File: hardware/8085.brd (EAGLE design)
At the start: 167.9 x 122.5 mm, 52 parts, among them IC10 74HCT00N, IC11 74HCT245DW, IC2 74AC573N, IC3 ATF16V8BP3, IC4 74AC00D, IC5 74HCT245DW, IC6 74AC273N, IC7 74HCT139N, IC8 7404N, IC9 74HCT138N

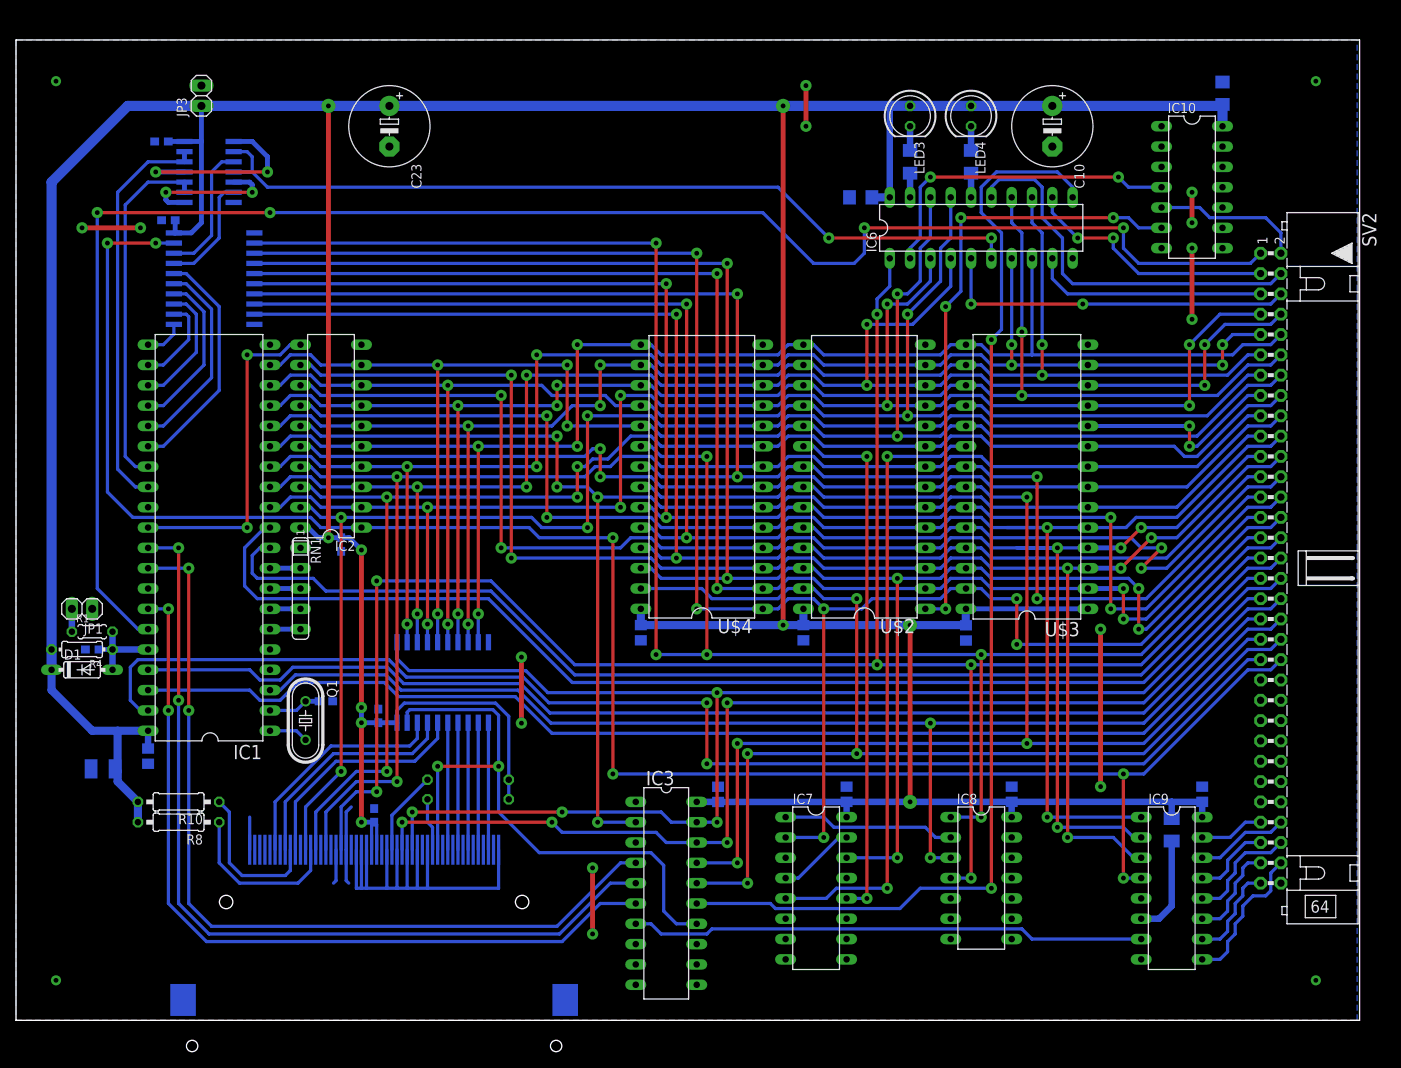
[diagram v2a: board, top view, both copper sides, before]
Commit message: Bug in PCB board design fixed
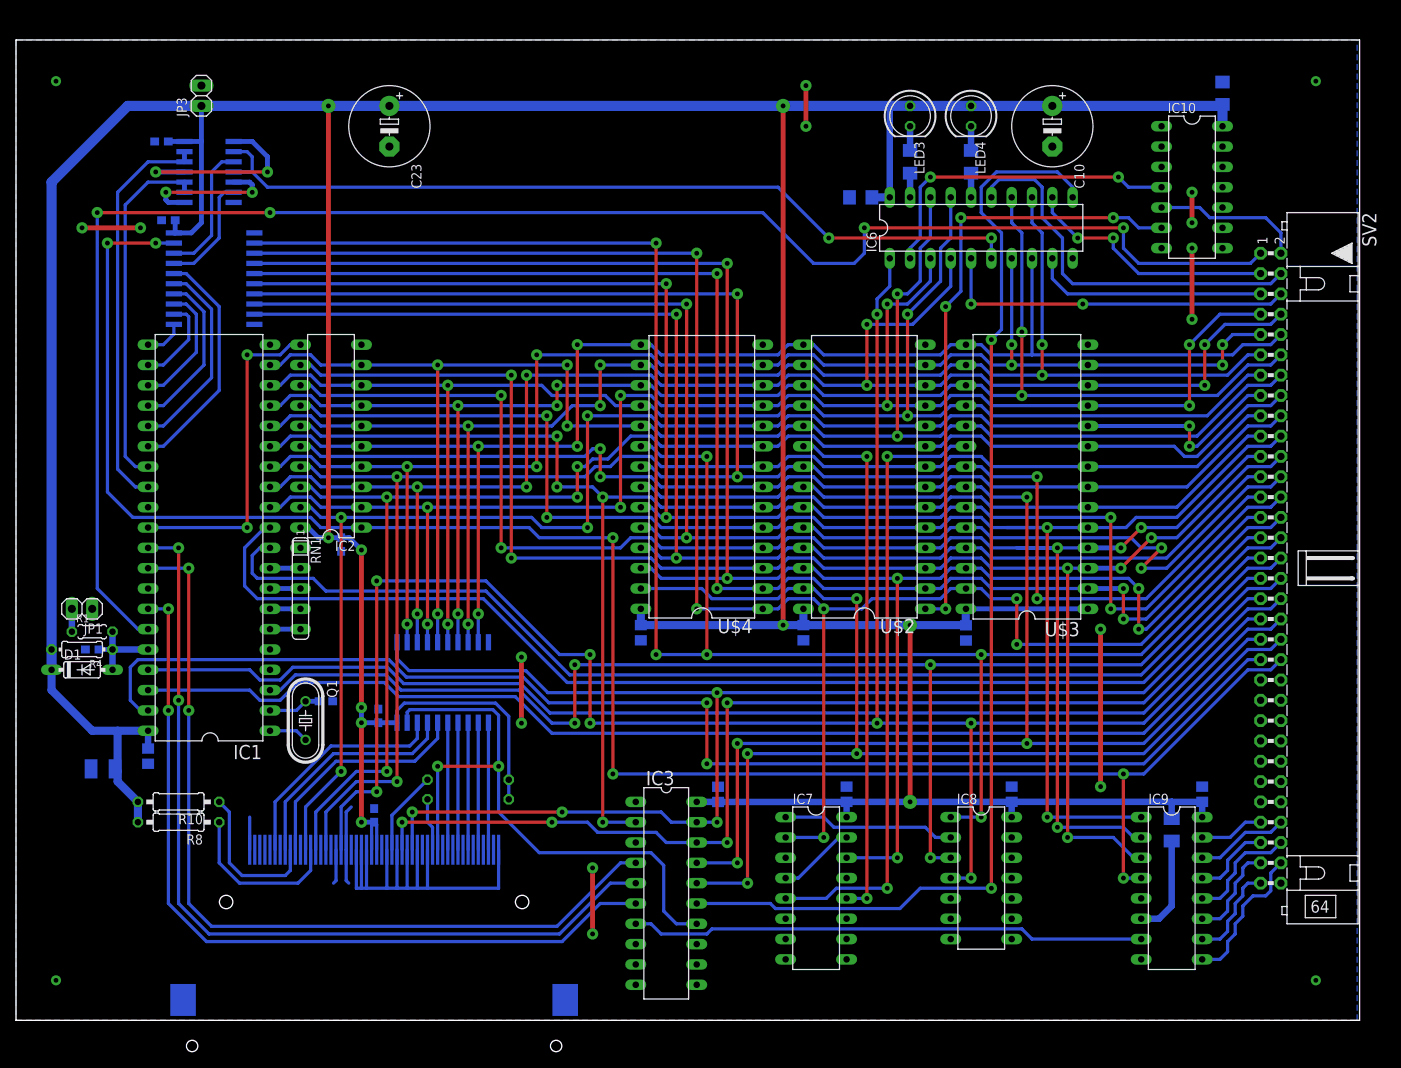
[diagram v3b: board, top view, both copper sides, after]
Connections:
- net !RESET: now also SV2.37; no longer SV2.31
- net RESET: now also SV2.31; no longer SV2.37
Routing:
- net RESET: track 151.9 -> 166.6 mm, vias 2 -> 4
- net !RESET: track 238.0 -> 245.9 mm, vias 6 -> 8
- net A4: track 179.1 -> 178.5 mm
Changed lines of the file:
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@@
 <contactref element="SV2" pad="32"/>
 <contactref element="IC1" pad="10"/>
-<wire x1="140.6525" y1="43.18" x2="69.85" y2="43.18" width="0.4064" layer="16"/>
+<wire x1="140.6525" y1="43.18" x2="69.215" y2="43.18" width="0.4064" layer="16"/>
 <wire x1="30.1625" y1="55.245" x2="29.5275" y2="55.88" width="0.4064" layer="16"/>
 <wire x1="29.5275" y1="55.88" x2="29.5275" y2="58.1025" width="0.4064" layer="16"/>
@@
 <wire x1="30.1625" y1="55.245" x2="37.1475" y2="55.245" width="0.4064" layer="16"/>
 <wire x1="37.1475" y1="55.245" x2="38.735" y2="53.6575" width="0.4064" layer="16"/>
-<wire x1="38.735" y1="53.6575" x2="59.3725" y2="53.6575" width="0.4064" layer="16"/>
-<wire x1="59.3725" y1="53.6575" x2="69.85" y2="43.18" width="0.4064" layer="16"/>
+<wire x1="38.735" y1="53.6575" x2="58.7375" y2="53.6575" width="0.4064" layer="16"/>
+<wire x1="58.7375" y1="53.6575" x2="69.215" y2="43.18" width="0.4064" layer="16"/>
 </signal>
 <signal name="VCC">
@@
 <wire x1="67.6275" y1="73.025" x2="67.6275" y2="66.675" width="0.4064" layer="1"/>
 <via x="67.6275" y="66.675" extent="1-16" drill="0.6" diameter="1.4224" shape="octagon"/>
-<via x="72.7075" y="65.405" extent="1-16" drill="0.6" diameter="1.4224" shape="octagon"/>
-<wire x1="72.7075" y1="65.405" x2="72.7075" y2="24.765" width="0.4064" layer="1"/>
-<via x="72.7075" y="24.765" extent="1-16" drill="0.6" diameter="1.4224" shape="octagon"/>
+<via x="73.3425" y="65.405" extent="1-16" drill="0.6" diameter="1.4224" shape="octagon"/>
+<wire x1="73.3425" y1="65.405" x2="73.3425" y2="24.765" width="0.4064" layer="1"/>
+<via x="73.3425" y="24.765" extent="1-16" drill="0.6" diameter="1.4224" shape="octagon"/>
 <contactref element="IC3" pad="2"/>
-<wire x1="72.7075" y1="24.765" x2="77.47" y2="24.765" width="0.4064" layer="16"/>
-<wire x1="67.6275" y1="66.675" x2="71.4375" y2="66.675" width="0.4064" layer="16"/>
-<wire x1="71.4375" y1="66.675" x2="72.7075" y2="65.405" width="0.4064" layer="16"/>
-<wire x1="72.7075" y1="65.405" x2="79.375" y2="65.405" width="0.4064" layer="16"/>
+<wire x1="73.3425" y1="24.765" x2="77.47" y2="24.765" width="0.4064" layer="16"/>
+<wire x1="67.6275" y1="66.675" x2="72.0725" y2="66.675" width="0.4064" layer="16"/>
+<wire x1="72.0725" y1="66.675" x2="73.3425" y2="65.405" width="0.4064" layer="16"/>
+<wire x1="73.3425" y1="65.405" x2="79.375" y2="65.405" width="0.4064" layer="16"/>
 <wire x1="38.1" y1="73.025" x2="67.6275" y2="73.025" width="0.4064" layer="16"/>
 </signal>
@@
 <wire x1="85.09" y1="22.225" x2="81.28" y2="22.225" width="0.4064" layer="16"/>
 <wire x1="81.28" y1="22.225" x2="80.01" y2="23.495" width="0.4064" layer="16"/>
-<wire x1="80.01" y1="23.495" x2="68.2625" y2="23.495" width="0.4064" layer="16"/>
 <wire x1="48.26" y1="21.32" x2="48.26" y2="24.765" width="0.4064" layer="16"/>
-<wire x1="68.2625" y1="23.495" x2="66.9925" y2="24.765" width="0.4064" layer="16"/>
+<wire x1="66.9925" y1="24.765" x2="71.4375" y2="24.765" width="0.4064" layer="16"/>
+<wire x1="71.4375" y1="24.765" x2="72.7075" y2="23.495" width="0.4064" layer="16"/>
+<wire x1="72.7075" y1="23.495" x2="80.01" y2="23.495" width="0.4064" layer="16"/>
 </signal>
 <signal name="MEM_WR">
@@
 </signal>
 <signal name="RESET">
-<contactref element="SV2" pad="37"/>
-<wire x1="153.9875" y1="50.165" x2="155.575" y2="50.165" width="0.4064" layer="16"/>
-<wire x1="140.97" y1="37.1475" x2="153.9875" y2="50.165" width="0.4064" layer="16"/>
-<wire x1="114.3" y1="37.1475" x2="140.97" y2="37.1475" width="0.4064" layer="16"/>
+<wire x1="114.3" y1="44.45" x2="140.6525" y2="44.45" width="0.4064" layer="16"/>
 <contactref element="IC1" pad="3"/>
 <contactref element="IC8" pad="3"/>
-<via x="114.3" y="37.1475" extent="1-16" drill="0.6" diameter="1.4224" shape="octagon"/>
-<wire x1="114.3" y1="37.1475" x2="114.3" y2="20.32" width="0.4064" layer="1"/>
+<via x="114.3" y="44.45" extent="1-16" drill="0.6" diameter="1.4224" shape="octagon"/>
+<wire x1="114.3" y1="44.45" x2="114.3" y2="20.32" width="0.4064" layer="1"/>
 <via x="114.3" y="20.32" extent="1-16" drill="0.6" diameter="1.4224" shape="octagon"/>
 <wire x1="114.3" y1="20.32" x2="116.84" y2="20.32" width="0.4064" layer="16"/>
-<wire x1="114.3" y1="37.1475" x2="66.8655" y2="37.1475" width="0.4064" layer="16"/>
 <wire x1="46.228" y1="43.18" x2="34.925" y2="43.18" width="0.4064" layer="16"/>
 <wire x1="34.925" y1="43.18" x2="33.02" y2="41.275" width="0.4064" layer="16"/>
 <wire x1="33.02" y1="41.275" x2="31.75" y2="41.275" width="0.4064" layer="16"/>
 <wire x1="46.228" y1="43.18" x2="48.133" y2="41.275" width="0.4064" layer="16"/>
-<wire x1="48.133" y1="41.275" x2="62.738" y2="41.275" width="0.4064" layer="16"/>
-<wire x1="62.738" y1="41.275" x2="66.8655" y2="37.1475" width="0.4064" layer="16"/>
+<wire x1="48.133" y1="41.275" x2="62.865" y2="41.275" width="0.4064" layer="16"/>
+<contactref element="SV2" pad="31"/>
+<wire x1="155.575" y1="57.785" x2="153.9875" y2="57.785" width="0.4064" layer="16"/>
+<wire x1="153.9875" y1="57.785" x2="140.6525" y2="44.45" width="0.4064" layer="16"/>
+<wire x1="114.3" y1="44.45" x2="69.85" y2="44.45" width="0.4064" layer="16"/>
+<via x="69.85" y="44.45" extent="1-16" drill="0.6" diameter="1.4224" shape="octagon"/>
+<wire x1="69.85" y1="44.45" x2="69.85" y2="37.1475" width="0.4064" layer="1"/>
+<via x="69.85" y="37.1475" extent="1-16" drill="0.6" diameter="1.4224" shape="octagon"/>
+<wire x1="69.85" y1="37.1475" x2="66.9925" y2="37.1475" width="0.4064" layer="16"/>
+<wire x1="66.9925" y1="37.1475" x2="62.865" y2="41.275" width="0.4064" layer="16"/>
 </signal>
 <signal name="!RESET">
-<via x="107.6325" y="44.45" extent="1-16" drill="0.6" diameter="1.4224" shape="octagon"/>
-<wire x1="107.6325" y1="44.45" x2="107.6325" y2="88.265" width="0.4064" layer="1"/>
+<via x="107.6325" y="37.1475" extent="1-16" drill="0.6" diameter="1.4224" shape="octagon"/>
+<wire x1="107.6325" y1="37.1475" x2="107.6325" y2="88.265" width="0.4064" layer="1"/>
 <via x="107.6325" y="88.265" extent="1-16" drill="0.6" diameter="1.4224" shape="octagon"/>
-<wire x1="155.575" y1="57.785" x2="153.9875" y2="57.785" width="0.4064" layer="16"/>
-<wire x1="140.6525" y1="44.45" x2="153.9875" y2="57.785" width="0.4064" layer="16"/>
-<contactref element="SV2" pad="31"/>
 <contactref element="IC6" pad="1"/>
 <wire x1="107.6325" y1="88.265" x2="107.6325" y2="90.17" width="0.4064" layer="16"/>
@@
 <wire x1="109.22" y1="91.7575" x2="109.22" y2="95.25" width="0.4064" layer="16"/>
 <contactref element="IC8" pad="4"/>
-<wire x1="107.6325" y1="44.45" x2="119.38" y2="44.45" width="0.4064" layer="16"/>
-<via x="119.38" y="44.45" extent="1-16" drill="0.6" diameter="1.4224" shape="octagon"/>
-<wire x1="119.38" y1="44.45" x2="119.38" y2="17.78" width="0.4064" layer="1"/>
+<wire x1="107.6325" y1="37.1475" x2="119.38" y2="37.1475" width="0.4064" layer="16"/>
+<via x="119.38" y="37.1475" extent="1-16" drill="0.6" diameter="1.4224" shape="octagon"/>
+<wire x1="119.38" y1="37.1475" x2="119.38" y2="17.78" width="0.4064" layer="1"/>
 <via x="119.38" y="17.78" extent="1-16" drill="0.6" diameter="1.4224" shape="octagon"/>
 <wire x1="119.38" y1="17.78" x2="116.84" y2="17.78" width="0.4064" layer="16"/>
-<wire x1="119.38" y1="44.45" x2="140.6525" y2="44.45" width="0.4064" layer="16"/>
-<wire x1="107.6325" y1="44.45" x2="69.85" y2="44.45" width="0.4064" layer="16"/>
+<wire x1="119.38" y1="37.1475" x2="140.97" y2="37.1475" width="0.4064" layer="16"/>
 <contactref element="CON1" pad="41"/>
 <via x="45.085" y="28.575" extent="1-16" drill="0.6" diameter="1.4224" shape="octagon"/>
@@
 <wire x1="45.085" y1="28.575" x2="42.545" y2="28.575" width="0.4064" layer="16"/>
 <wire x1="42.545" y1="28.575" x2="40.64" y2="26.67" width="0.4064" layer="16"/>
-<wire x1="45.085" y1="54.9275" x2="59.3725" y2="54.9275" width="0.4064" layer="16"/>
-<wire x1="59.3725" y1="54.9275" x2="69.85" y2="44.45" width="0.4064" layer="16"/>
+<contactref element="SV2" pad="37"/>
+<wire x1="155.575" y1="50.165" x2="153.9875" y2="50.165" width="0.4064" layer="16"/>
+<wire x1="153.9875" y1="50.165" x2="140.97" y2="37.1475" width="0.4064" layer="16"/>
+<wire x1="45.085" y1="54.9275" x2="58.7375" y2="54.9275" width="0.4064" layer="16"/>
+<wire x1="58.7375" y1="54.9275" x2="67.945" y2="45.72" width="0.4064" layer="16"/>
+<wire x1="67.945" y1="45.72" x2="71.755" y2="45.72" width="0.4064" layer="16"/>
+<via x="71.755" y="45.72" extent="1-16" drill="0.6" diameter="1.4224" shape="octagon"/>
+<wire x1="71.755" y1="45.72" x2="71.755" y2="37.1475" width="0.4064" layer="1"/>
+<via x="71.755" y="37.1475" extent="1-16" drill="0.6" diameter="1.4224" shape="octagon"/>
+<wire x1="71.755" y1="37.1475" x2="107.6325" y2="37.1475" width="0.4064" layer="16"/>
 </signal>
 <signal name="SET_BANK_A14">
@@
 <signal name="INTA">
 <contactref element="SV2" pad="33"/>
-<wire x1="69.5325" y1="42.2275" x2="140.97" y2="42.2275" width="0.4064" layer="16"/>
+<wire x1="68.8975" y1="42.2275" x2="140.97" y2="42.2275" width="0.4064" layer="16"/>
 <wire x1="140.97" y1="42.2275" x2="153.9875" y2="55.245" width="0.4064" layer="16"/>
 <wire x1="153.9875" y1="55.245" x2="155.575" y2="55.245" width="0.4064" layer="16"/>
@@
 <wire x1="28.575" y1="59.055" x2="31.115" y2="61.595" width="0.4064" layer="16"/>
 <wire x1="31.75" y1="61.595" x2="31.115" y2="61.595" width="0.4064" layer="16"/>
-<wire x1="30.1625" y1="52.705" x2="59.055" y2="52.705" width="0.4064" layer="16"/>
-<wire x1="59.055" y1="52.705" x2="69.5325" y2="42.2275" width="0.4064" layer="16"/>
+<wire x1="30.1625" y1="52.705" x2="58.42" y2="52.705" width="0.4064" layer="16"/>
+<wire x1="58.42" y1="52.705" x2="68.8975" y2="42.2275" width="0.4064" layer="16"/>
 </signal>
 <signal name="LOCAL_IO_CS">

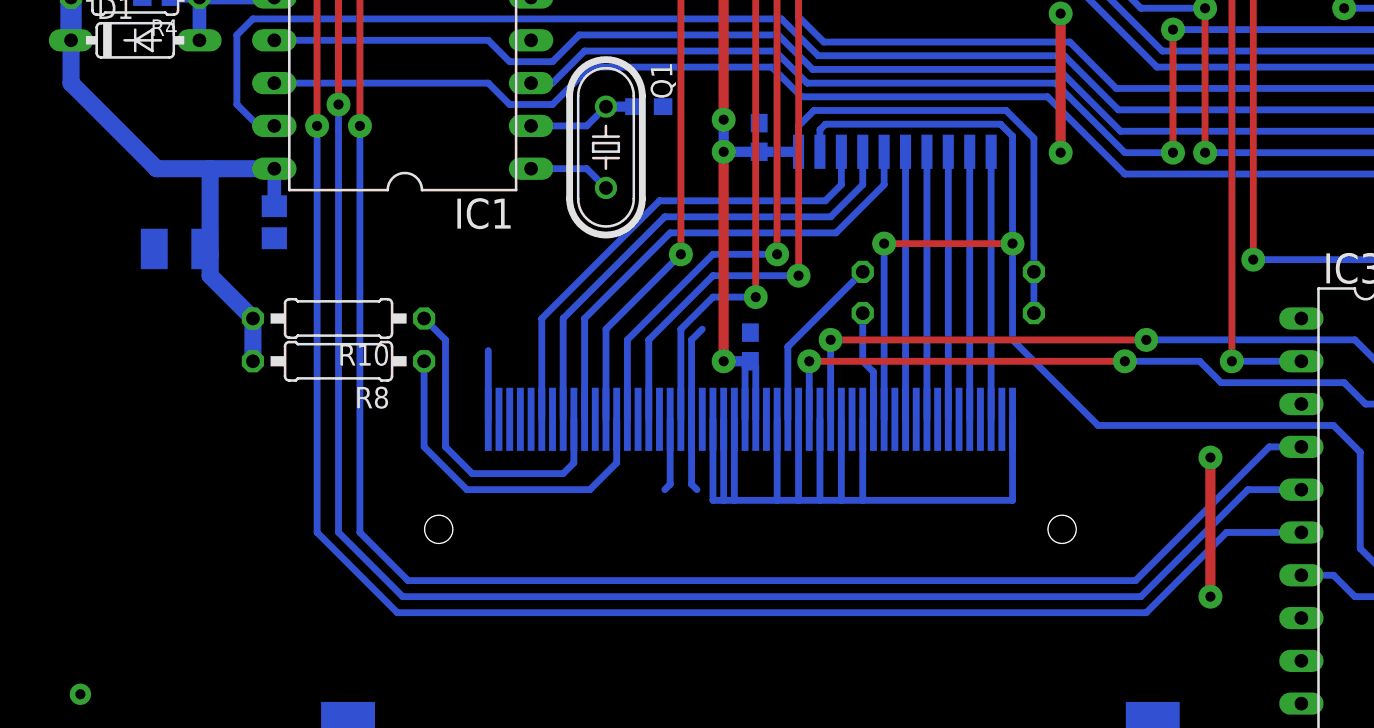
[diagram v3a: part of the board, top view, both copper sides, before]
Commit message: CF indicator LED added to CPU board
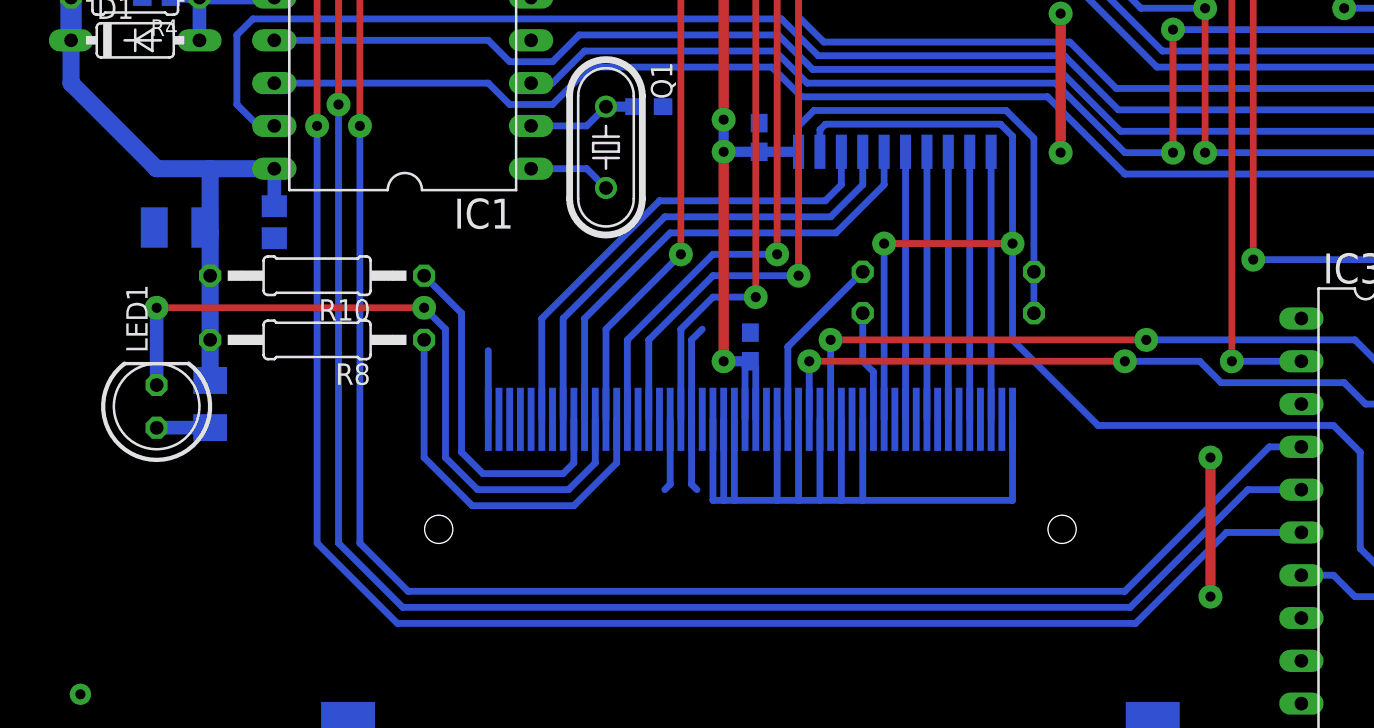
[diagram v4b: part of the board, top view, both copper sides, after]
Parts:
- added LED1: (no value), led:LED5MM
- added R5: (no value), rcl:M1206
- R10, R8: device rcl:0207/10 -> rcl:0207/12
- moved R10 2.84 mm to (19.1, 29.8)
- moved R8 1.80 mm to (19.1, 26.0)
- moved C16 1.27 mm to (10.9, 32.7)
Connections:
- new net N$15: LED1.A, R5.1
- new net N$16: CON1.45, LED1.K
- net VCC: now also R5.2
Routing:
- net N$16: track 0.00 -> 42.8 mm, vias 0 -> 2
- net N$15: track 0.00 -> 3.18 mm
- net N$11: track 20.8 -> 23.2 mm
- net N$13: track 19.3 -> 21.4 mm
- net RD: track 107.3 -> 108.2 mm
- net WR: track 109.6 -> 110.5 mm
- net IO_M: track 101.7 -> 102.6 mm
